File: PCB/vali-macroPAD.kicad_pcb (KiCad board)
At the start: 2 copper layers, 114.3 x 59.5 mm, 29 parts, among them M3 MountingHole_3.2mm_M3, SW1 SW_Push, SW10 RotaryEncoder_Switch, SW11 SW_Push, SW12 SW_Push, SW2 SW_Push, SW3 SW_Push, SW4 SW_Push, SW5 SW_Push, SW6 SW_Push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

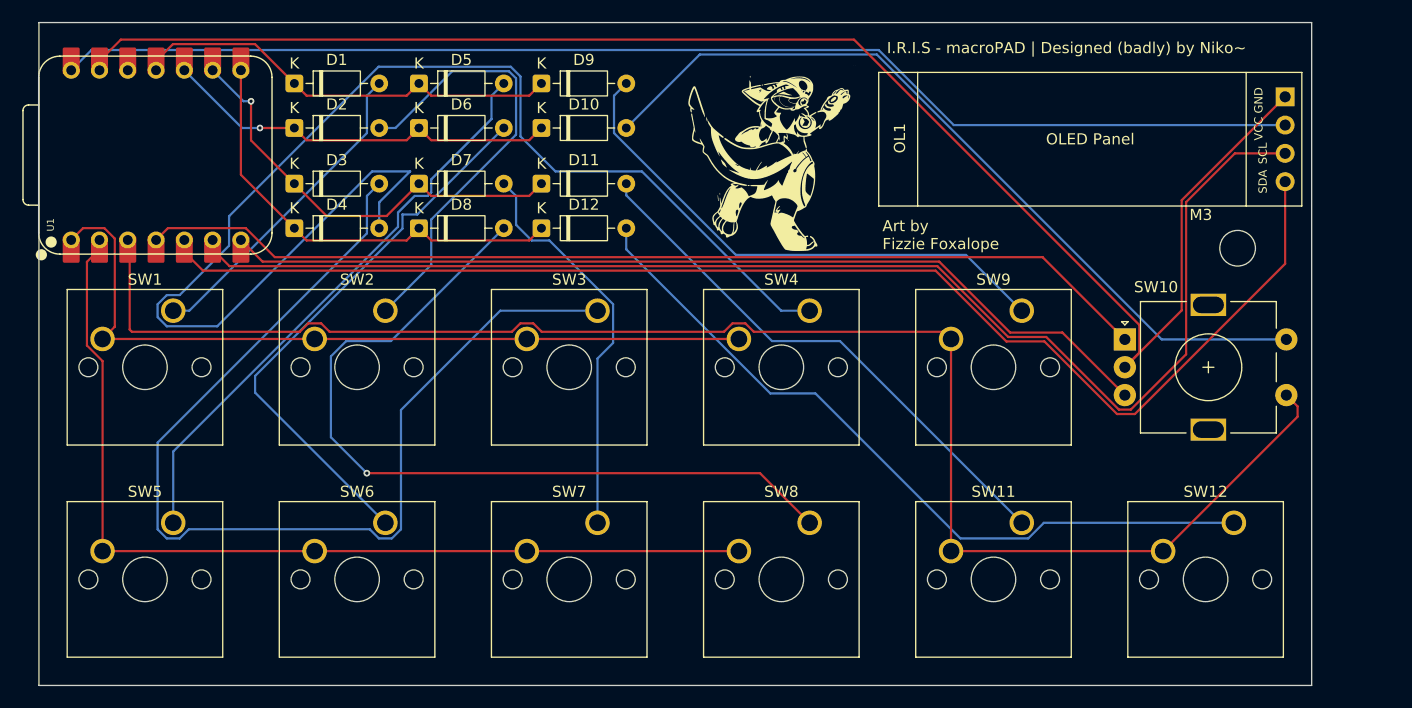
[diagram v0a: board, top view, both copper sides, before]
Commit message: Tidied up wire routes
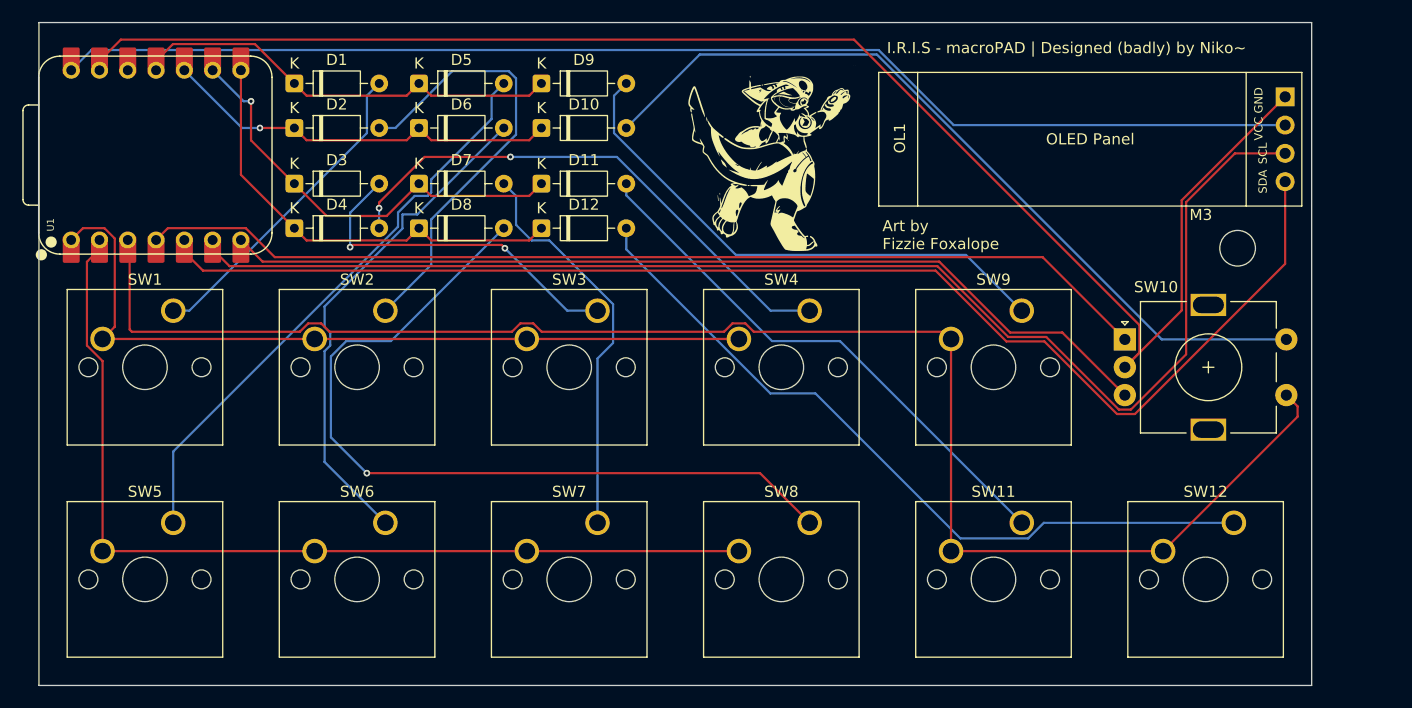
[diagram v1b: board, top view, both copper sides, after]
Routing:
- net Net-(D4-A): track 117.4 -> 48.4 mm, vias 0 -> 2
- net Net-(D3-A): track 94.5 -> 31.5 mm, vias 0 -> 2
- net Net-(D6-A): track 50.3 -> 45.6 mm
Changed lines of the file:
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@@
 	)
 	(segment
-		(start 114.667075 91.267075)
-		(end 114.667075 92.759575)
+		(start 120.9 89.043814)
+		(end 120.9 98.9925)
 		(width 0.2)
 		(layer "B.Cu")
@@
 	)
 	(segment
-		(start 114.667075 92.759575)
+		(start 120.9 98.9925)
 		(end 126.365 104.4575)
+		(width 0.2)
+		(layer "B.Cu")
+		(net 3)
+	)
+	(segment
+		(start 120.9 86.851186)
+		(end 121.416 87.367186)
+		(width 0.2)
+		(layer "B.Cu")
+		(net 3)
+	)
+	(segment
+		(start 121.416 87.367186)
+		(end 121.416 88.527814)
+		(width 0.2)
+		(layer "B.Cu")
+		(net 3)
+	)
+	(segment
+		(start 120.9 85.03415)
+		(end 120.9 86.851186)
+		(width 0.2)
+		(layer "B.Cu")
+		(net 3)
+	)
+	(segment
+		(start 127.901 78.03315)
+		(end 120.9 85.03415)
+		(width 0.2)
+		(layer "B.Cu")
+		(net 3)
+	)
+	(segment
+		(start 121.416 88.527814)
+		(end 120.9 89.043814)
+		(width 0.2)
+		(layer "B.Cu")
+		(net 3)
+	)
+	(segment
+		(start 127.901 76.7661)
+		(end 127.901 78.03315)
 		(width 0.2)
 		(layer "B.Cu")
@@
 		(start 129.2339 76.7661)
 		(end 127.901 76.7661)
-		(width 0.2)
-		(layer "B.Cu")
-		(net 3)
-	)
-	(segment
-		(start 127.901 78.03315)
-		(end 114.667075 91.267075)
-		(width 0.2)
-		(layer "B.Cu")
-		(net 3)
-	)
-	(segment
-		(start 127.901 76.7661)
-		(end 127.901 78.03315)
 		(width 0.2)
 		(layer "B.Cu")
@@
 	)
 	(segment
-		(start 106.734686 105.8585)
-		(end 105.914 105.037814)
-		(width 0.2)
-		(layer "B.Cu")
+		(start 137.1 79.8)
+		(end 136.802 79.502)
+		(width 0.2)
+		(layer "F.Cu")
 		(net 25)
 	)
 	(segment
-		(start 136.68144 85.4075)
-		(end 127.766 94.32294)
-		(width 0.2)
-		(layer "B.Cu")
+		(start 136.802 79.502)
+		(end 123.399 79.502)
+		(width 0.2)
+		(layer "F.Cu")
 		(net 25)
 	)
 	(segment
-		(start 107.895314 105.8585)
-		(end 106.734686 105.8585)
-		(width 0.2)
-		(layer "B.Cu")
+		(start 123.399 79.502)
+		(end 123.2 79.701)
+		(width 0.2)
+		(layer "F.Cu")
 		(net 25)
 	)
-	(segment
-		(start 125.784686 105.8585)
-		(end 124.964 105.037814)
-		(width 0.2)
-		(layer "B.Cu")
+	(via
+		(at 137.1 79.8)
+		(size 0.6)
+		(drill 0.3)
+		(layers "F.Cu" "B.Cu")
 		(net 25)
 	)
-	(segment
-		(start 105.914 105.037814)
-		(end 105.914 97.25105)
-		(width 0.2)
-		(layer "B.Cu")
+	(via
+		(at 123.2 79.701)
+		(size 0.6)
+		(drill 0.3)
+		(layers "F.Cu" "B.Cu")
 		(net 25)
 	)
 	(segment
-		(start 105.914 97.25105)
-		(end 124.709 78.45605)
+		(start 142.7075 85.4075)
+		(end 137.1 79.8)
 		(width 0.2)
 		(layer "B.Cu")
@@
 	)
 	(segment
+		(start 123.2 79.701)
+		(end 123.2 76.61)
+		(width 0.2)
+		(layer "B.Cu")
+		(net 25)
+	)
+	(segment
 		(start 145.415 85.4075)
-		(end 136.68144 85.4075)
+		(end 142.7075 85.4075)
 		(width 0.2)
 		(layer "B.Cu")
@@
 	)
 	(segment
-		(start 108.716 105.037814)
-		(end 107.895314 105.8585)
+		(start 123.2 76.61)
+		(end 125.81 74)
 		(width 0.2)
 		(layer "B.Cu")
@@
 	)
 	(segment
-		(start 124.964 105.037814)
-		(end 108.716 105.037814)
-		(width 0.2)
-		(layer "B.Cu")
-		(net 25)
-	)
-	(segment
-		(start 127.766 105.037814)
-		(end 126.945314 105.8585)
-		(width 0.2)
-		(layer "B.Cu")
-		(net 25)
-	)
-	(segment
-		(start 124.709 75.101)
-		(end 125.81 74)
-		(width 0.2)
-		(layer "B.Cu")
-		(net 25)
-	)
-	(segment
-		(start 124.709 78.45605)
-		(end 124.709 75.101)
-		(width 0.2)
-		(layer "B.Cu")
-		(net 25)
-	)
-	(segment
-		(start 126.945314 105.8585)
-		(end 125.784686 105.8585)
-		(width 0.2)
-		(layer "B.Cu")
-		(net 25)
-	)
-	(segment
-		(start 127.766 94.32294)
-		(end 127.766 105.037814)
-		(width 0.2)
-		(layer "B.Cu")
-		(net 25)
-	)
-	(segment
-		(start 125.81 75.68384)
+		(start 129.89384 71.6)
+		(end 125.8 75.69384)
+		(width 0.2)
+		(layer "F.Cu")
+		(net 26)
+	)
+	(segment
+		(start 137.6 71.6)
+		(end 129.89384 71.6)
+		(width 0.2)
+		(layer "F.Cu")
+		(net 26)
+	)
+	(segment
+		(start 125.8 75.69384)
+		(end 125.8 76.2)
+		(width 0.2)
+		(layer "F.Cu")
+		(net 26)
+	)
+	(via
+		(at 125.8 76.2)
+		(size 0.6)
+		(drill 0.3)
+		(layers "F.Cu" "B.Cu")
+		(net 26)
+	)
+	(via
+		(at 137.6 71.6)
+		(size 0.6)
+		(drill 0.3)
+		(layers "F.Cu" "B.Cu")
+		(net 26)
+	)
+	(segment
+		(start 125.8 77.99)
 		(end 125.81 78)
 		(width 0.2)
@@
 	)
 	(segment
-		(start 137.62215 63.498)
-		(end 125.75495 63.498)
+		(start 125.8 76.2)
+		(end 125.8 77.99)
 		(width 0.2)
 		(layer "B.Cu")
@@
 	)
 	(segment
-		(start 112.32825 79.573564)
-		(end 107.895314 84.0065)
+		(start 147.15705 71.6)
+		(end 137.6 71.6)
 		(width 0.2)
 		(layer "B.Cu")
@@
 	)
 	(segment
-		(start 112.32825 76.9247)
-		(end 112.32825 79.573564)
+		(start 164.465 85.4075)
+		(end 160.96455 85.4075)
 		(width 0.2)
 		(layer "B.Cu")
@@
 	)
 	(segment
-		(start 106.734686 86.8085)
-		(end 111.26766 86.8085)
-		(width 0.2)
-		(layer "B.Cu")
-		(net 26)
-	)
-	(segment
-		(start 164.465 85.4075)
-		(end 161.9075 85.4075)
-		(width 0.2)
-		(layer "B.Cu")
-		(net 26)
-	)
-	(segment
-		(start 141.64006 72.899)
-		(end 138.502 69.76094)
-		(width 0.2)
-		(layer "B.Cu")
-		(net 26)
-	)
-	(segment
-		(start 106.734686 84.0065)
-		(end 105.914 84.827186)
-		(width 0.2)
-		(layer "B.Cu")
-		(net 26)
-	)
-	(segment
-		(start 161.9075 85.4075)
-		(end 149.399 72.899)
-		(width 0.2)
-		(layer "B.Cu")
-		(net 26)
-	)
-	(segment
-		(start 125.17716 72.899)
-		(end 128.59484 72.899)
-		(width 0.2)
-		(layer "B.Cu")
-		(net 26)
-	)
-	(segment
-		(start 111.26766 86.8085)
-		(end 125.17716 72.899)
-		(width 0.2)
-		(layer "B.Cu")
-		(net 26)
-	)
-	(segment
-		(start 138.502 69.76094)
-		(end 138.502 64.37785)
-		(width 0.2)
-		(layer "B.Cu")
-		(net 26)
-	)
-	(segment
-		(start 105.914 84.827186)
-		(end 105.914 85.987814)
-		(width 0.2)
-		(layer "B.Cu")
-		(net 26)
-	)
-	(segment
-		(start 149.399 72.899)
-		(end 141.64006 72.899)
-		(width 0.2)
-		(layer "B.Cu")
-		(net 26)
-	)
-	(segment
-		(start 107.895314 84.0065)
-		(end 106.734686 84.0065)
-		(width 0.2)
-		(layer "B.Cu")
-		(net 26)
-	)
-	(segment
-		(start 128.59484 72.899)
-		(end 125.81 75.68384)
-		(width 0.2)
-		(layer "B.Cu")
-		(net 26)
-	)
-	(segment
-		(start 138.502 64.37785)
-		(end 137.62215 63.498)
-		(width 0.2)
-		(layer "B.Cu")
-		(net 26)
-	)
-	(segment
-		(start 125.75495 63.498)
-		(end 112.32825 76.9247)
-		(width 0.2)
-		(layer "B.Cu")
-		(net 26)
-	)
-	(segment
-		(start 105.914 85.987814)
-		(end 106.734686 86.8085)
-		(width 0.2)
-		(layer "B.Cu")
+		(start 160.96455 85.4075)
+		(end 147.15705 71.6)
+		(width 0.2)
+		(layer "B.Cu")

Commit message: tidied up wire routes
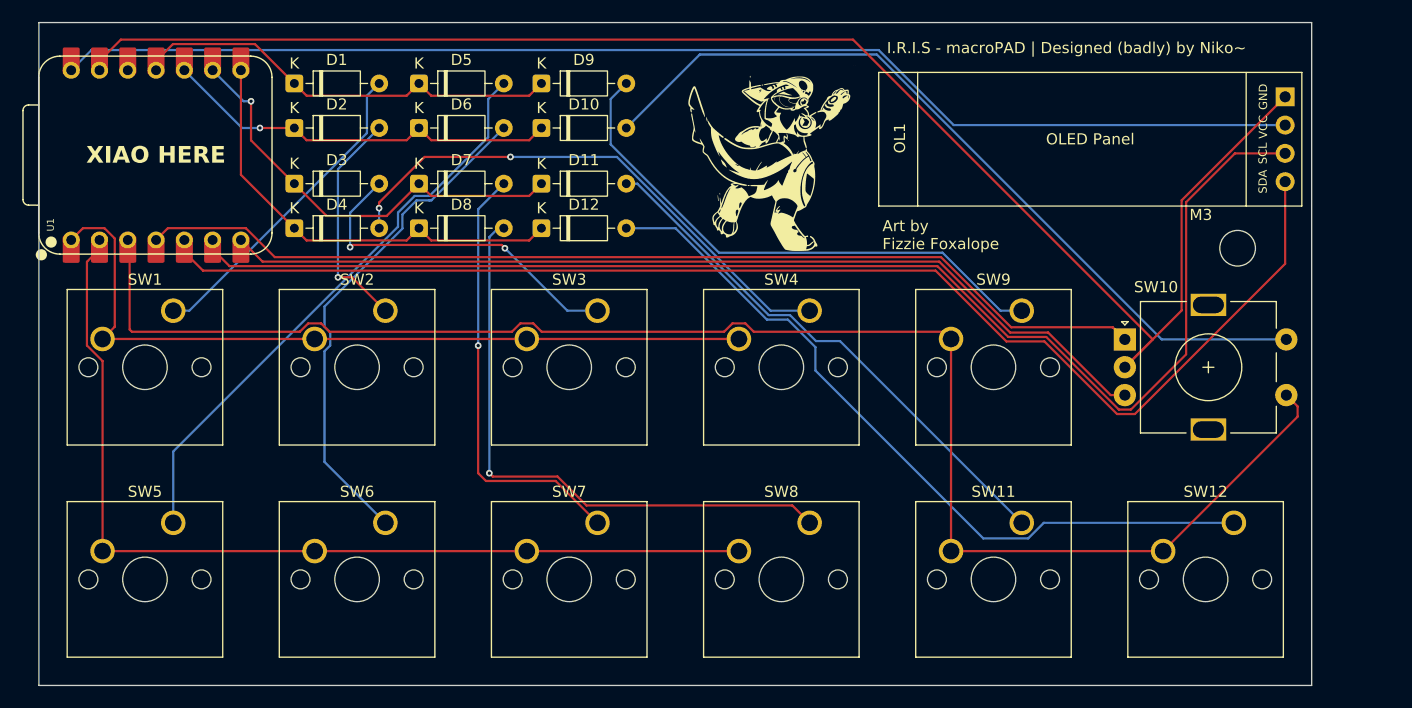
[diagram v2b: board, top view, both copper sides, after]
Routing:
- net Net-(D8-A): track 73.7 -> 53.4 mm
- net Net-(D2-A): track 40.4 -> 20.4 mm, vias 0 -> 1
- net Net-(D7-A): track 36.0 -> 39.5 mm, vias 0 -> 1
- net Net-(D9-A): track 48.1 -> 49.2 mm
- net GND: track 139.4 -> 140.3 mm
- net Net-(D11-A): track 48.7 -> 48.1 mm
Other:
- board text added: "XIAO HERE"
- board text added: "macroPAD Designed : 6-12-2025 By : Niko~ Version : 1.4.1"
- board text removed: "macroPAD Designed : 6-12-2025 By : Niko~ Version : 1.4"
